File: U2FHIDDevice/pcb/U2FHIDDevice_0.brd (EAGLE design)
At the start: 48.3 x 25.4 mm, 31 parts, among them CN1 STLINKV2_SWD_IF_, CN2 TE-1734028, SW1 SKRPACE010, SW2 SKRPACE010, U1 STM32F411RET6, U2 LD39050PU33R, U3 USBLC6-2SC6, X1 NX3215SA-32.768K

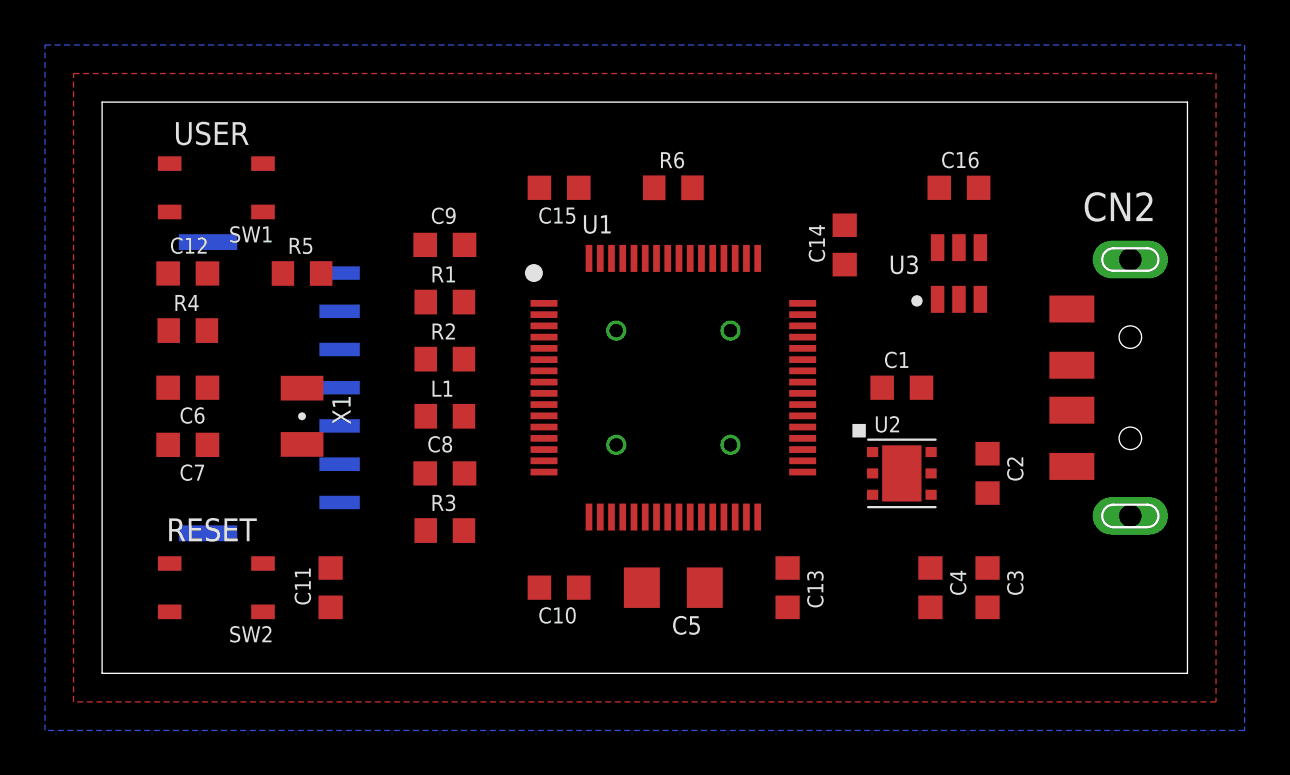
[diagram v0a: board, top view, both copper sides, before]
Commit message: 回路図／基板デザインを修正
・ユーザーボタンを削除（不要なので）
・通信処理中を表すLEDを追加
・プリント基板サイズを縮小
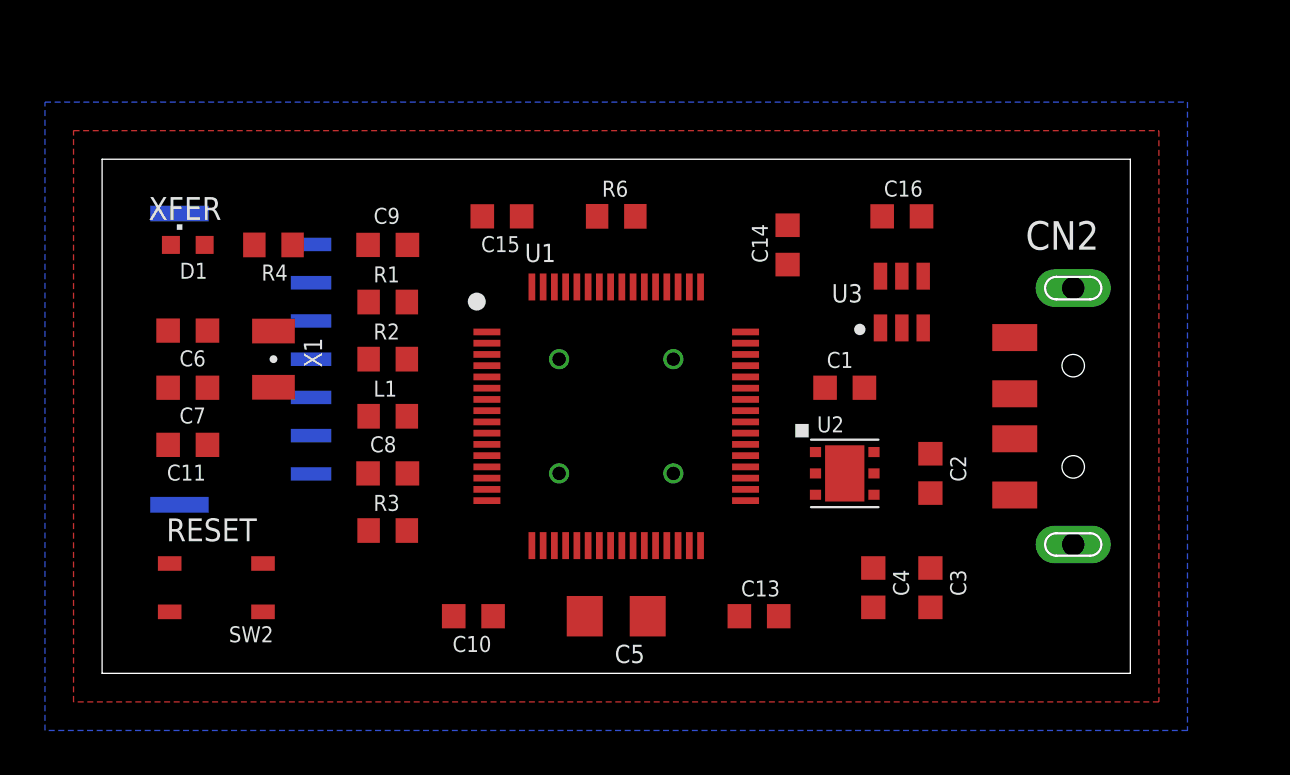
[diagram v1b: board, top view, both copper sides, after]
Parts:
- removed C12: 0.1uF, Parts:C0603K
- removed R5: 100, Parts:R0603
- removed SW1: SKRPACE010, Parts:SKRPACE010
- added D1: WE_150060VS55040, Parts:CHIPLED_0603
- R4: value 4.7k -> 510
- moved C11 8.98 mm to (3.81, 10.2), turned to 180 degrees
- moved R4 5.39 mm to (7.62, 19.1), turned to 180 degrees
- moved C10 4.02 mm to (16.5, 2.54)
- moved X1 2.84 mm to (7.62, 14.0)
- moved C15 2.84 mm to (17.8, 20.3)
- moved C16 2.84 mm to (35.6, 20.3)
- moved C5 2.84 mm to (22.9, 2.54)
- moved CN2 2.84 mm to (43.2, 11.4)
- moved R6 2.84 mm to (22.9, 20.3)
- moved U1 2.84 mm to (22.9, 11.4)
- moved U3 2.84 mm to (35.6, 16.5)
- moved C14 2.54 mm to (30.5, 19.1)
- moved C6 2.54 mm to (3.81, 15.2)
- moved C8 2.54 mm to (12.7, 8.89)
- moved C9 2.54 mm to (12.7, 19.1)
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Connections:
- removed net USER_BUTTON: C12.1, R4.1, SW1.1, SW1.2, U1.2
- new net USER_LED: R4.1, U1.21
- net 0V: now also D1.C; no longer R5.2, SW1.3, SW1.4
- net N$1: now also D1.A, R4.2; no longer C12.2, R5.1
- net VDD: no longer R4.2
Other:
- board size 48.3 x 25.4 mm -> 45.7 x 22.9 mm
- board text added: "XFER"
- board text removed: "USER"

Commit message: 回路図／基板デザインを修正
・青色LEDを追加（One Cardと通信中に点灯させる想定）
・回路が間違っていたので修正
・リセットボタン、LDOの位置を修正
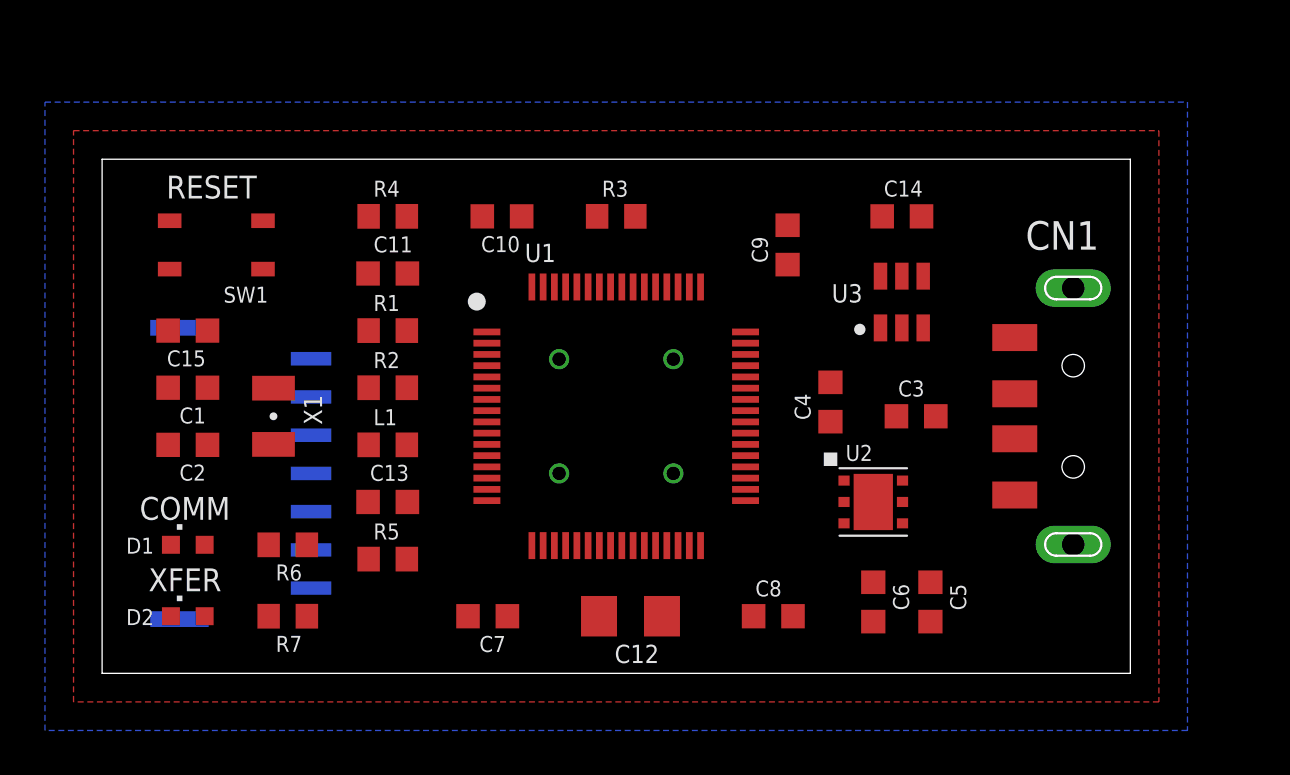
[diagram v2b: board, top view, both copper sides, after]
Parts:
- removed C16: 0.1uF, Parts:C0603K
- removed SW2: SKRPACE010, Parts:SKRPACE010
- added C12: 4.7uF, Parts:C1206
- added D2: APHD1608LQBC/D, Parts:CHIPLED_0603
- added R5: 0, Parts:R0603
- added R7: 680, Parts:R0603
- added SW1: SKRPACE010, Parts:SKRPACE010
- C1: value 0.1uF -> 2.7pF
- C11: value 0.1uF -> 1uF
- C2: value 1uF -> 2.7pF
- C5: value 4.7uF -> 1uF; device Parts:C1206 -> Parts:C0603K
- C6, C7: value 2.7pF -> 0.1uF
- C9: value 1uF -> 0.1uF
- CN1: value STLINKV2_SWD_IF_ -> TE-1734028; device Connectors:DF65-7P-1.7V_DEV -> Connectors:TE-1734028
- CN2: value TE-1734028 -> STLINKV2_SWD_IF_; device Connectors:TE-1734028 -> Connectors:DF65-7P-1.7V_DEV
- D1: value WE_150060VS55040 -> APTD1608LCGCK
- R3: value 0 -> 10k
- R4: value 510 -> 10k
- R6: value 10k -> 1k
- moved CN1 34.4 mm to (43.2, 11.4), flipped to the top
- moved CN2 34.4 mm to (8.89, 8.89), flipped to the bottom
- moved C2 33.0 mm to (3.81, 10.2), turned to 180 degrees
- moved C6 32.8 mm to (34.3, 3.17), turned to 270 degrees
- moved C1 29.2 mm to (3.81, 12.7), turned to 180 degrees
- moved R6 20.7 mm to (8.26, 5.71), turned to 180 degrees
- moved C8 18.3 mm to (29.8, 2.54), turned to 0 degrees
- moved C10 17.8 mm to (17.8, 20.3)
- moved C9 17.8 mm to (30.5, 19.1), turned to 90 degrees
- moved C13 17.3 mm to (12.7, 7.62), turned to 180 degrees
- moved R3 17.3 mm to (22.9, 20.3)
- moved C7 16.8 mm to (17.1, 2.54)
- moved C15 14.9 mm to (3.81, 15.2)
- moved C5 14.0 mm to (36.8, 3.17), turned to 270 degrees
- moved D1 13.3 mm to (3.81, 5.71)
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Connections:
- removed net USER_LED: R4.1, U1.21
- removed net VBAT: C9.1, U1.1
- new net LED_BLUE: R7.1, U1.22
- new net LED_GREEN: R6.1, U1.21
- new net N$4: D2.A, R7.2
- new net USER_BUTTON: R4.1, U1.2
- net 0V: now also C12.2, C8.2, CN1.FG1, CN1.FG2, CN1.P$4, CN2.2, D2.C, R3.2, R5.1, SW1.3, SW1.4; no longer C13.2, C16.2, CN1.2, CN2.FG1, CN2.FG2, CN2.P$4, R3.1, R6.2, SW2.3, SW2.4
- net AGND: now also C13.2, R5.2; no longer C8.2, R3.2
- net AVDD: now also C13.1; no longer C8.1
- net BOOT0: now also R3.1; no longer R6.1
- net N$1: now also R6.2; no longer R4.2
- net N$2: now also C1.1; no longer C6.1
- net N$3: now also C2.1; no longer C7.1
- net NRST: now also C15.1, CN2.4, SW1.1, SW1.2; no longer C11.1, CN1.4, SW2.1, SW2.2
- net SWO: now also CN2.5; no longer CN1.5
- net TCK: now also CN2.1; no longer CN1.1
- net TMS: now also CN2.3; no longer CN1.3
- net U5V: now also C14.1, C3.1, C4.1, CN1.P$1; no longer C1.1, C16.1, C2.1, CN2.P$1
- net USART_RX: now also CN2.7; no longer CN1.7
- net USART_TX: now also CN2.6; no longer CN1.6
- net USB_DM: now also CN1.P$2; no longer CN2.P$2
- net USB_DP: now also CN1.P$3; no longer CN2.P$3
- net VCAP_1: now also C12.1; no longer C5.1
- net VDD: now also C11.1, C5.1, C6.1, C7.1, C8.1, C9.1, R4.2, U1.1; no longer C13.1, C14.1, C15.1, C3.1, C4.1
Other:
- board text added: "COMM"

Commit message: 回路図／基板デザインを修正
・実体配線を考慮し、部品配置を修正
・配線が間違っていたので修正（ESD保護回路の部分）
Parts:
- moved C14 17.8 mm to (36.2, 2.54)
- moved C5 15.9 mm to (36.2, 19.1), turned to 90 degrees
- moved C6 15.9 mm to (33.7, 19.1), turned to 90 degrees
- moved U3 10.8 mm to (34.9, 5.71), turned to 90 degrees
- moved U2 7.01 mm to (34.9, 14.6), turned to 180 degrees
- moved C4 4.55 mm to (36.5, 10.2), turned to 270 degrees
- moved C3 2.84 mm to (33.7, 10.2), turned to 270 degrees
- turned R4 to 180 degrees
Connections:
- new net UDM: CN1.P$2, U3.3
- new net UDP: CN1.P$3, U3.1
- net USB_DM: no longer CN1.P$2, U3.3
- net USB_DP: no longer CN1.P$3, U3.1
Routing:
- net VDD: track 0.00 -> 20.3 mm
- net USER_BUTTON: track 0.00 -> 9.59 mm
- net N$2: track 0.00 -> 8.23 mm
- net N$3: track 0.00 -> 8.22 mm
- net NRST: track 0.00 -> 7.58 mm
- net OSC32_IN: track 0.00 -> 4.00 mm
- net OSC32_OUT: track 0.00 -> 3.97 mm
- net BOOT0: track 0.00 -> 3.51 mm
- net VCAP_1: track 0.00 -> 3.44 mm
- net N$4: track 0.00 -> 2.85 mm
- net N$1: track 0.00 -> 2.85 mm

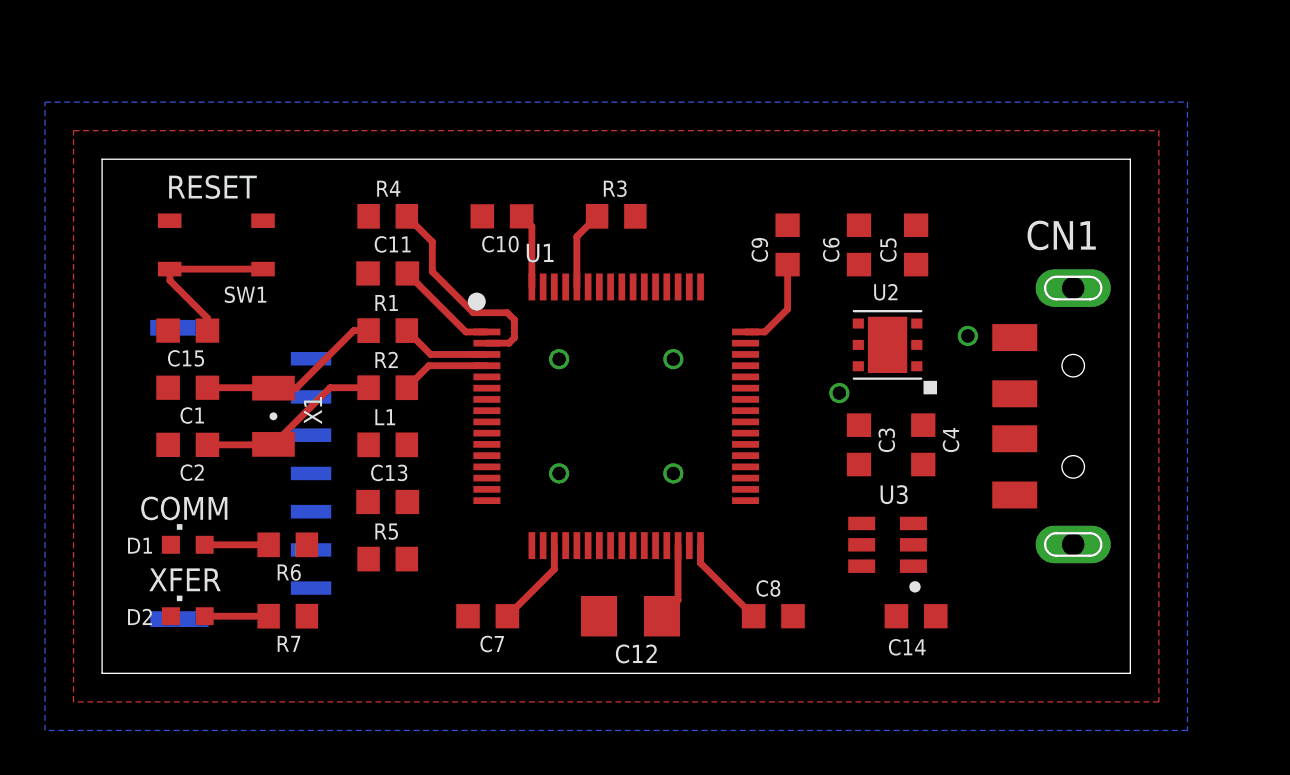
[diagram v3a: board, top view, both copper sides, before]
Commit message: 回路図／基板デザインを修正
・実体配線ずみ
・ST-LINK
V2-1インターフェースを背面パッドではなく、スルーホールに修正しました（スルーホールテストワイヤーで接続可能とするための措置）
・一部IC、クリスタルのパッド面積を拡張（手はんだを可能とするための措置）
・部品表、ガーバーデータを出力
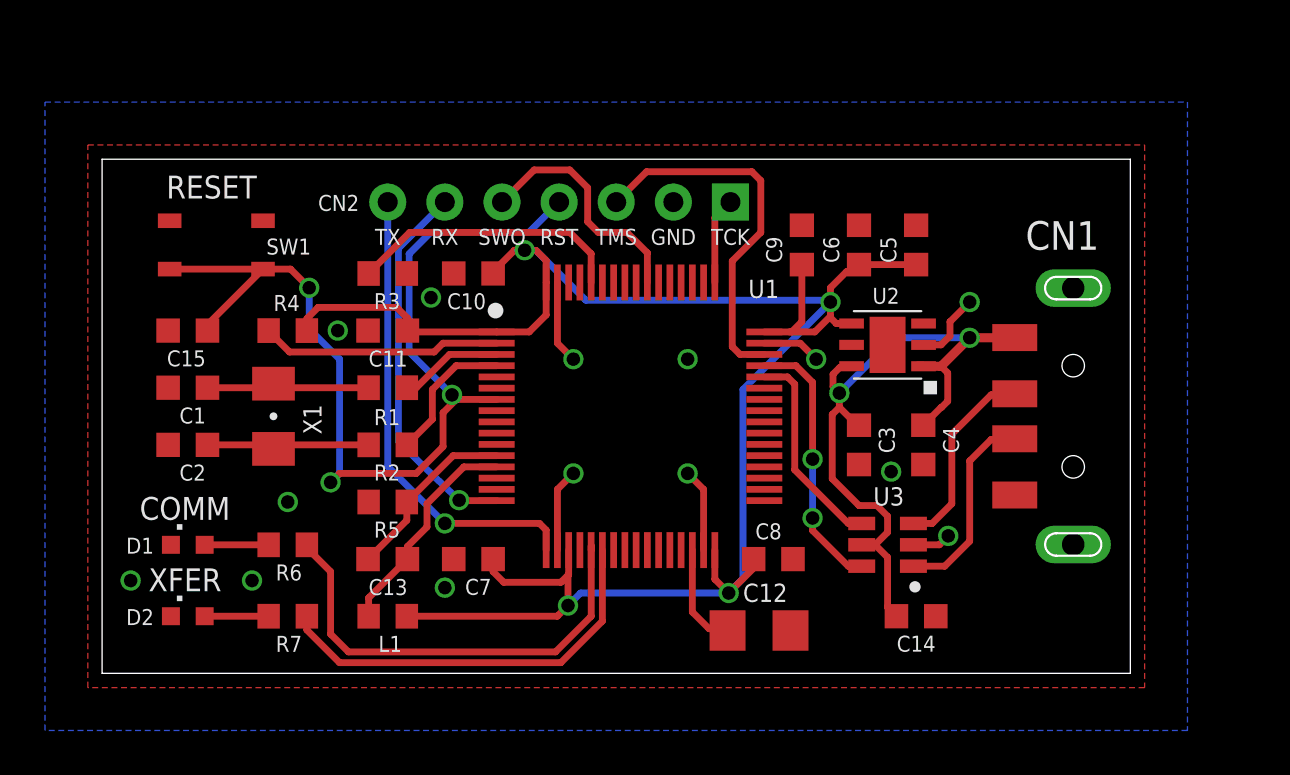
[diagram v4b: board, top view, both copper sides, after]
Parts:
- CN2: value STLINKV2_SWD_IF_ -> IF_7PIN; device Connectors:DF65-7P-1.7V_DEV -> Connectors:HEADER_7PIN
- U1: value STM32F411RET6 -> STM32F411RET6_; device Parts:LQFP64-10X10 -> Parts:LQFP64-10X10_DEV
- U2: value LD39050PU33R -> LD39050PU33R_DEV; device Parts:DFN6-3X3 -> Parts:DFN6-3X3_DEV
- X1: value NX3215SA-32.768K -> NX3215SA_; device Parts:NX3215 -> Parts:NX3215_DEV
- moved CN2 22.5 mm to (27.9, 21.0), flipped to the top, turned to 180 degrees
- moved R3 10.5 mm to (12.7, 17.8)
- moved L1 7.62 mm to (12.7, 2.54), turned to 180 degrees
- moved R4 6.75 mm to (8.26, 15.2), turned to 0 degrees
- moved C12 5.75 mm to (29.2, 1.91), turned to 0 degrees
- moved C10 2.84 mm to (16.5, 17.8)
- moved C7 2.62 mm to (16.5, 5.08)
- moved C11 2.54 mm to (12.7, 15.2)
- moved R1 2.54 mm to (12.7, 12.7)
- moved C13 2.54 mm to (12.7, 5.08)
- moved C8 2.54 mm to (29.8, 5.08)
- moved R5 2.54 mm to (12.7, 7.62)
- moved R2 2.54 mm to (12.7, 10.2)
- moved U1 0.64 mm to (23.5, 11.4)
- moved C9 0.63 mm to (31.1, 19.1)
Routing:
- net VDD: track 20.3 -> 85.9 mm, vias 0 -> 4
- net NRST: track 7.58 -> 44.4 mm, vias 0 -> 3
- net U5V: track 0.00 -> 31.1 mm
- net USART_RX: track 0.00 -> 20.9 mm, vias 0 -> 1
- net LED_GREEN: track 0.00 -> 20.3 mm
- net 0V: track 0.00 -> 18.8 mm, vias 4 -> 14
- net LED_BLUE: track 0.00 -> 18.3 mm
- net USART_TX: track 0.00 -> 16.9 mm, vias 0 -> 1
- net TMS: track 0.00 -> 16.6 mm
- net USB_DP: track 0.00 -> 11.9 mm, vias 0 -> 2
- net SWO: track 0.00 -> 10.8 mm
- net AVDD: track 0.00 -> 9.86 mm
- net USB_DM: track 0.00 -> 9.26 mm
- net UDP: track 0.00 -> 8.94 mm
- net BOOT0: track 3.51 -> 12.3 mm
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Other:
- board text added: "GND"
- board text added: "RST"
- board text added: "RX"
- board text added: "SWO"
- board text added: "TCK"
- board text added: "TMS"
- board text added: "TX"
